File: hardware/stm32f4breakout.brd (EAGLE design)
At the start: 132.1 x 53.3 mm, 18 parts, among them U101 STM32F427VGT6, X101 24MHz

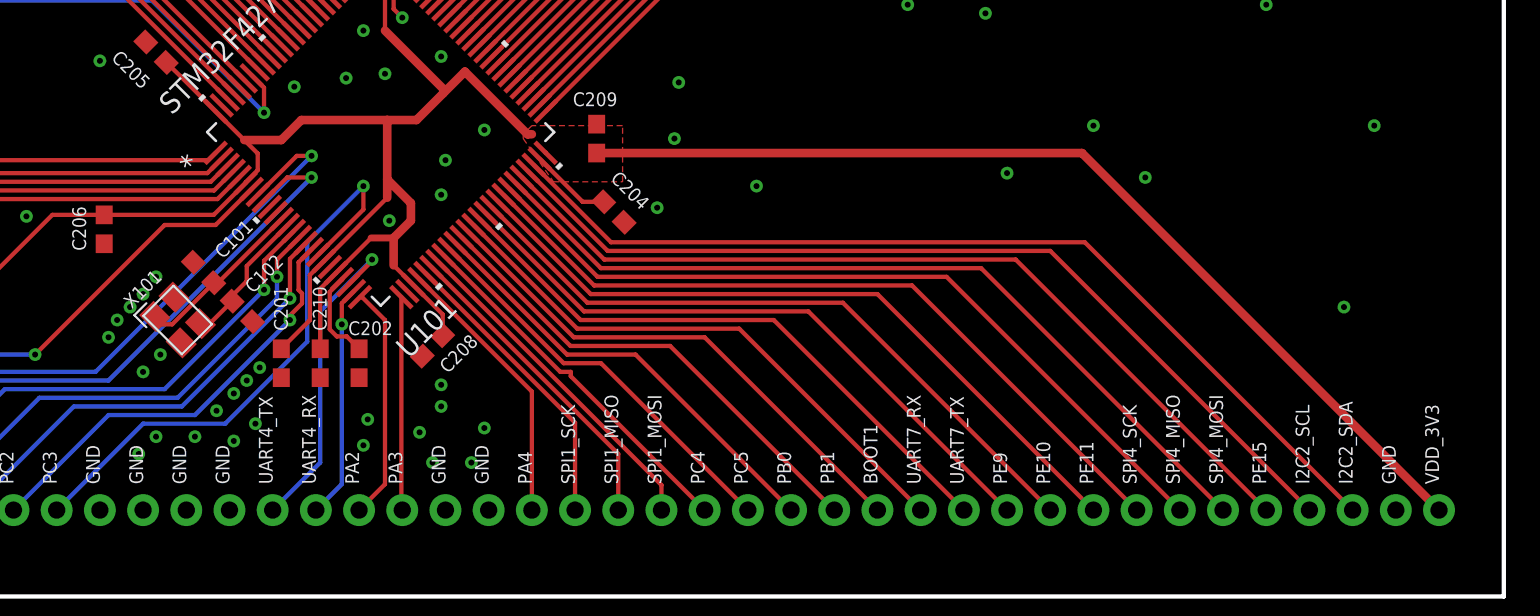
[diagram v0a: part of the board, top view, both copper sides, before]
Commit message: Add 4.7uF decoupling cap
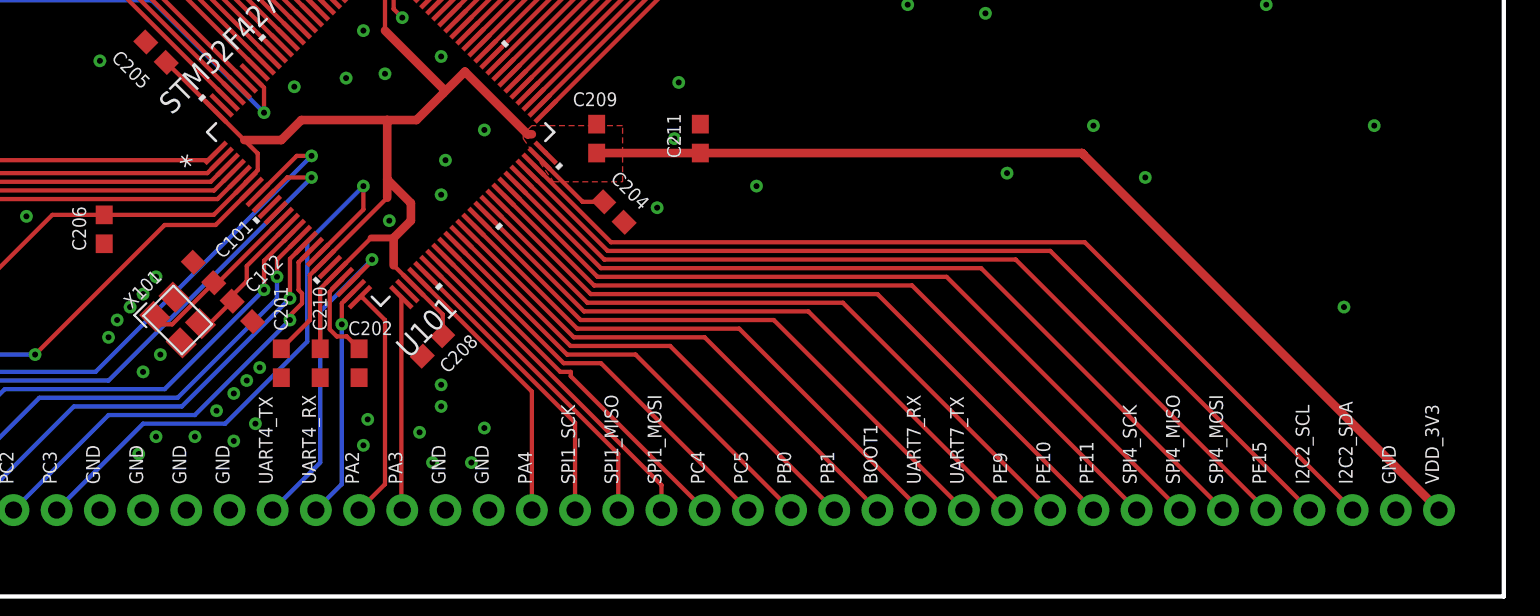
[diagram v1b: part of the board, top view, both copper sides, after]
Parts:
- added C211: 4.7uF, quad:C0603
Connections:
- net GND: now also C211.2
- net VDD_3V3: now also C211.1
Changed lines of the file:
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@@
 <attribute name="NAME" x="62.865" y="15.621" size="0.8128" layer="25" rot="R90"/>
+</element>
+<element name="C211" library="quad" package="C0603" value="4.7uF" x="84.836" y="26.924" smashed="yes" rot="R90">
+<attribute name="NAME" x="83.693" y="25.781" size="0.8128" layer="25" rot="R90"/>
 </element>
 </elements>
@@
 <via x="58.928" y="13.462" extent="1-16" drill="0.35"/>
 <via x="50.038" y="15.24" extent="1-16" drill="0.35"/>
+<contactref element="C211" pad="2"/>
 </signal>
 <signal name="UART4_TX">
@@
 <wire x1="66.802" y1="19.471928125" x2="67.964459375" y2="18.30946875" width="0.254" layer="1"/>
 <wire x1="75.742634375" y1="26.08764375" x2="75.756278125" y2="26.074" width="0.254" layer="1"/>
-<wire x1="78.74" y1="26.074" x2="107.276" y2="26.074" width="0.508" layer="1"/>
-<wire x1="107.276" y1="26.074" x2="128.27" y2="5.08" width="0.508" layer="1"/>
+<wire x1="107.38175625" y1="25.96824375" x2="107.276" y2="26.074" width="0.508" layer="1"/>
+<wire x1="107.38175625" y1="25.96824375" x2="128.27" y2="5.08" width="0.508" layer="1"/>
 <wire x1="67.257353125" y1="37.007634375" x2="66.294" y2="36.04428125" width="0.254" layer="1"/>
 <wire x1="66.294" y1="36.04428125" x2="66.294" y2="33.274" width="0.254" layer="1"/>
@@
 <wire x1="61.8752" y1="16.24578125" x2="60.198" y2="14.56858125" width="0.254" layer="1"/>
 <wire x1="62.484" y1="18.09214375" x2="62.484" y2="14.566" width="0.254" layer="1"/>
-<wire x1="50.171871875" y1="22.44" x2="49.784" y2="22.44" width="0.254" layer="1"/>
-<wire x1="50.171871875" y1="22.44" x2="56.225253125" y2="22.44" width="0.254" layer="1"/>
+<wire x1="49.784" y1="22.44" x2="56.225253125" y2="22.44" width="0.254" layer="1"/>
 <wire x1="56.225253125" y1="22.44" x2="58.105128125" y2="24.319875" width="0.254" layer="1"/>
 <wire x1="63.761984375" y1="18.663021875" x2="63.781996875" y2="18.6430125" width="0.254" layer="1"/>
@@
 <wire x1="36.83" y1="12.534" x2="46.736" y2="22.44" width="0.254" layer="1"/>
 <wire x1="46.736" y1="22.44" x2="49.784" y2="22.44" width="0.254" layer="1"/>
+<contactref element="C211" pad="1"/>
+<wire x1="78.74" y1="26.074" x2="84.836" y2="26.074" width="0.508" layer="1"/>
+<wire x1="84.836" y1="26.074" x2="107.276" y2="26.074" width="0.508" layer="1"/>
+<wire x1="107.276" y1="26.074" x2="107.38175625" y2="25.96824375" width="0.508" layer="1"/>
 <wire x1="58.105128125" y1="24.319875" x2="59.872896875" y2="22.552109375" width="0" layer="19" extent="1-1"/>
 <wire x1="63.761984375" y1="18.663021875" x2="63.40843125" y2="19.016575" width="0" layer="19" extent="1-1"/>

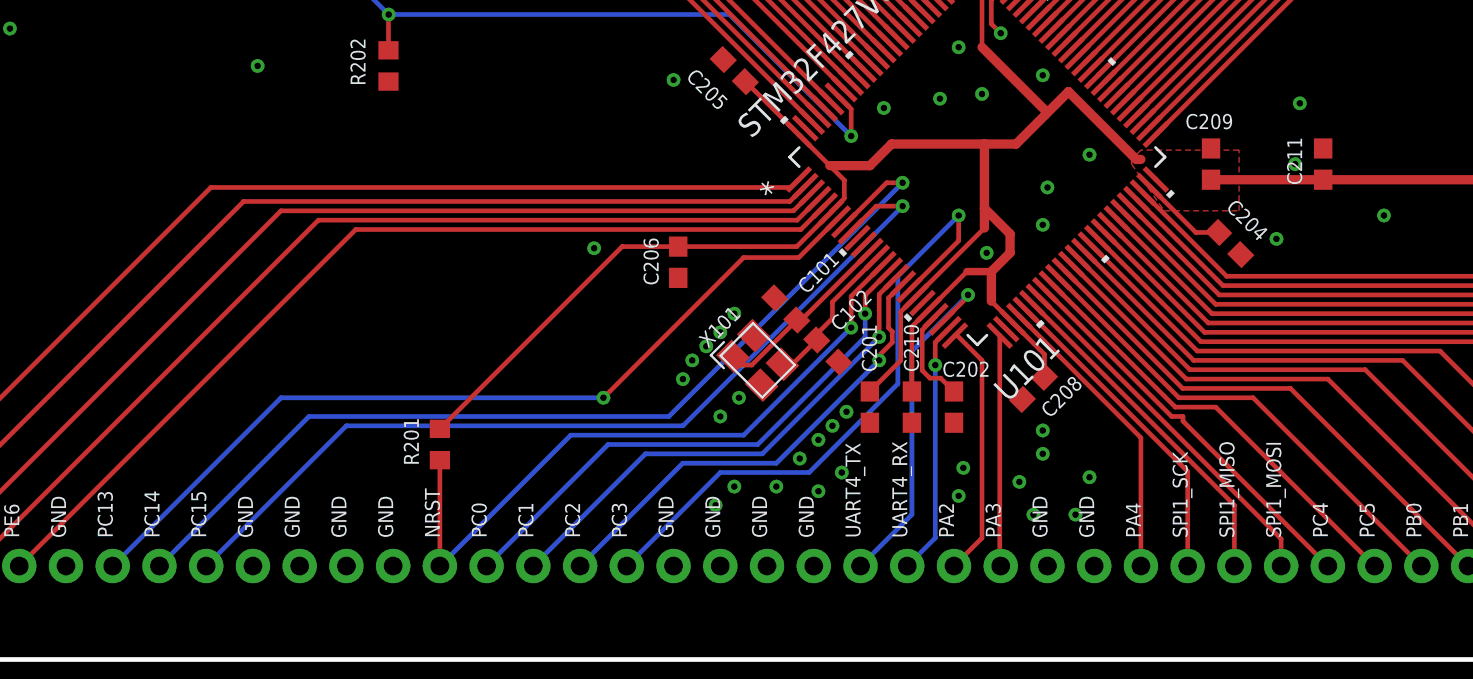
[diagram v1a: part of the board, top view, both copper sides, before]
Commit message: Fix final airwires on breakout, add DRC file
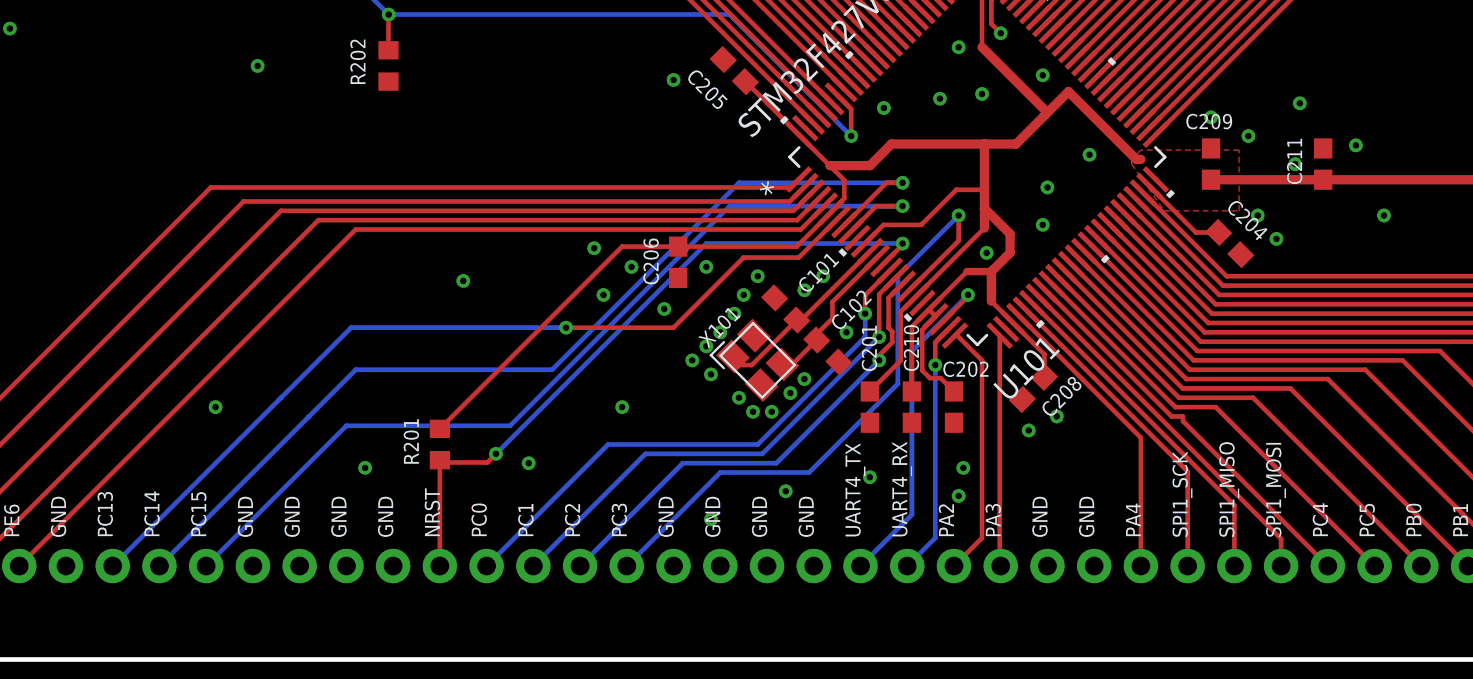
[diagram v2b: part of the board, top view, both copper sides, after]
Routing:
- net VDD_3V3: track 168.0 -> 176.3 mm
- net NRST: track 37.7 -> 37.4 mm, vias 1 -> 2
- net GND: vias 61 -> 72
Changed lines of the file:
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@@
 <via x="50.546" y="16.256" extent="1-16" drill="0.35"/>
 <via x="53.086" y="14.224" extent="1-16" drill="0.35"/>
-<via x="52.07" y="13.208" extent="1-16" drill="0.35"/>
-<via x="52.832" y="9.398" extent="1-16" drill="0.35"/>
-<via x="51.816" y="8.382" extent="1-16" drill="0.35"/>
-<via x="55.118" y="9.398" extent="1-16" drill="0.35"/>
-<via x="56.388" y="10.922" extent="1-16" drill="0.35"/>
-<via x="58.674" y="10.16" extent="1-16" drill="0.35"/>
-<via x="57.404" y="9.144" extent="1-16" drill="0.35"/>
+<via x="55.626" y="9.144" extent="1-16" drill="0.35"/>
+<via x="51.562" y="7.62" extent="1-16" drill="0.35"/>
 <via x="45.212" y="22.352" extent="1-16" drill="0.35"/>
 <via x="65.278" y="10.414" extent="1-16" drill="0.35"/>
 <via x="65.024" y="8.89" extent="1-16" drill="0.35"/>
-<via x="69.596" y="12.446" extent="1-16" drill="0.35"/>
-<via x="69.596" y="11.176" extent="1-16" drill="0.35"/>
-<via x="68.326" y="9.652" extent="1-16" drill="0.35"/>
-<via x="72.136" y="9.906" extent="1-16" drill="0.35"/>
-<via x="71.374" y="7.874" extent="1-16" drill="0.35"/>
-<via x="69.088" y="7.874" extent="1-16" drill="0.35"/>
+<via x="68.834" y="12.446" extent="1-16" drill="0.35"/>
+<via x="70.358" y="13.208" extent="1-16" drill="0.35"/>
 <via x="107.95" y="27.686" extent="1-16" drill="0.35"/>
 <via x="110.998" y="24.638" extent="1-16" drill="0.35"/>
@@
 <wire x1="66.802" y1="35.845175" x2="66.802" y2="34.544" width="0.254" layer="1"/>
 <via x="69.596" y="31.75" extent="1-16" drill="0.35"/>
-<via x="58.166" y="12.7" extent="1-16" drill="0.35"/>
-<via x="57.404" y="11.938" extent="1-16" drill="0.35"/>
-<via x="58.928" y="13.462" extent="1-16" drill="0.35"/>
-<via x="50.038" y="15.24" extent="1-16" drill="0.35"/>
 <contactref element="C211" pad="2"/>
+<via x="51.562" y="15.494" extent="1-16" drill="0.35"/>
+<via x="53.848" y="13.462" extent="1-16" drill="0.35"/>
+<via x="55.88" y="14.478" extent="1-16" drill="0.35"/>
+<via x="56.642" y="15.24" extent="1-16" drill="0.35"/>
+<via x="54.864" y="13.462" extent="1-16" drill="0.35"/>
+<via x="54.102" y="20.828" extent="1-16" drill="0.35"/>
+<via x="53.34" y="19.812" extent="1-16" drill="0.35"/>
+<via x="56.642" y="20.066" extent="1-16" drill="0.35"/>
+<via x="57.658" y="20.828" extent="1-16" drill="0.35"/>
+<via x="58.928" y="17.78" extent="1-16" drill="0.35"/>
+<via x="49.022" y="19.05" extent="1-16" drill="0.35"/>
+<via x="51.308" y="21.336" extent="1-16" drill="0.35"/>
+<via x="47.244" y="21.336" extent="1-16" drill="0.35"/>
+<via x="45.72" y="19.812" extent="1-16" drill="0.35"/>
+<via x="60.198" y="9.906" extent="1-16" drill="0.35"/>
+<via x="78.74" y="29.464" extent="1-16" drill="0.35"/>
+<via x="80.772" y="28.448" extent="1-16" drill="0.35"/>
+<via x="86.614" y="27.94" extent="1-16" drill="0.35"/>
+<via x="81.28" y="24.13" extent="1-16" drill="0.35"/>
+<via x="38.1" y="20.574" extent="1-16" drill="0.35"/>
+<via x="24.638" y="13.716" extent="1-16" drill="0.35"/>
+<via x="32.766" y="10.414" extent="1-16" drill="0.35"/>
+<via x="46.736" y="13.716" extent="1-16" drill="0.35"/>
+<via x="41.656" y="10.668" extent="1-16" drill="0.35"/>
 </signal>
 <signal name="UART4_TX">
@@
 <contactref element="U101" pad="8"/>
 <contactref element="J301" pad="8"/>
-<wire x1="58.812234375" y1="23.61276875" x2="61.107465625" y2="25.908" width="0.254" layer="1"/>
+<wire x1="61.107465625" y1="25.908" x2="58.812234375" y2="23.61276875" width="0.254" layer="1"/>
 <wire x1="61.107465625" y1="25.908" x2="61.976" y2="25.908" width="0.254" layer="1"/>
 <via x="61.976" y="25.908" extent="1-16" drill="0.35"/>
-<wire x1="61.976" y1="25.908" x2="49.276" y2="13.208" width="0.254" layer="16"/>
-<wire x1="29.718" y1="13.208" x2="21.59" y2="5.08" width="0.254" layer="16"/>
-<wire x1="49.276" y1="13.208" x2="29.718" y2="13.208" width="0.254" layer="16"/>
+<wire x1="29.673953125" y1="13.163953125" x2="29.718" y2="13.208" width="0.254" layer="16"/>
+<wire x1="29.673953125" y1="13.163953125" x2="21.59" y2="5.08" width="0.254" layer="16"/>
+<wire x1="53.086" y1="25.908" x2="42.926" y2="15.748" width="0.254" layer="16"/>
+<wire x1="42.926" y1="15.748" x2="32.258" y2="15.748" width="0.254" layer="16"/>
+<wire x1="32.258" y1="15.748" x2="29.673953125" y2="13.163953125" width="0.254" layer="16"/>
+<wire x1="61.976" y1="25.908" x2="53.086" y2="25.908" width="0.254" layer="16"/>
 </signal>
 <signal name="PC15">
@@
 <wire x1="60.544575" y1="24.638" x2="61.976" y2="24.638" width="0.254" layer="1"/>
 <via x="61.976" y="24.638" extent="1-16" drill="0.35"/>
-<wire x1="61.976" y1="24.638" x2="50.038" y2="12.7" width="0.254" layer="16"/>
 <wire x1="31.75" y1="12.7" x2="24.13" y2="5.08" width="0.254" layer="16"/>
-<wire x1="50.038" y1="12.7" x2="31.75" y2="12.7" width="0.254" layer="16"/>
+<wire x1="61.976" y1="24.638" x2="58.42" y2="24.638" width="0.254" layer="16"/>
+<wire x1="58.42" y1="24.638" x2="58.166" y2="24.638" width="0.254" layer="16"/>
+<wire x1="58.42" y1="24.638" x2="52.578" y2="24.638" width="0.254" layer="16"/>
+<wire x1="40.64" y1="12.7" x2="31.75" y2="12.7" width="0.254" layer="16"/>
+<wire x1="52.578" y1="24.638" x2="40.64" y2="12.7" width="0.254" layer="16"/>
 </signal>
 <signal name="CAN1_RX">
@@
 <contactref element="J301" pad="7"/>
 <wire x1="58.45868125" y1="23.966321875" x2="56.336359375" y2="21.844" width="0.254" layer="1"/>
-<via x="45.72" y="14.224" extent="1-16" drill="0.35"/>
-<wire x1="45.72" y1="14.224" x2="28.194" y2="14.224" width="0.254" layer="16"/>
-<wire x1="28.194" y1="14.224" x2="19.05" y2="5.08" width="0.254" layer="16"/>
+<wire x1="28.050115625" y1="14.080115625" x2="28.194" y2="14.224" width="0.254" layer="16"/>
+<wire x1="28.050115625" y1="14.080115625" x2="19.05" y2="5.08" width="0.254" layer="16"/>
 <wire x1="56.336359375" y1="21.844" x2="53.34" y2="21.844" width="0.254" layer="1"/>
-<wire x1="53.34" y1="21.844" x2="45.72" y2="14.224" width="0.254" layer="1"/>
+<wire x1="53.34" y1="21.844" x2="49.53" y2="18.034" width="0.254" layer="1"/>
+<wire x1="49.53" y1="18.034" x2="43.688" y2="18.034" width="0.254" layer="1"/>
+<via x="43.688" y="18.034" extent="1-16" drill="0.35"/>
+<wire x1="43.688" y1="18.034" x2="32.004" y2="18.034" width="0.254" layer="16"/>
+<wire x1="32.004" y1="18.034" x2="28.194" y2="14.224" width="0.254" layer="16"/>
 </signal>
 <signal name="PE2">
@@
 <contactref element="R201" pad="1"/>
 <contactref element="J301" pad="14"/>
-<wire x1="60.93355625" y1="21.49145" x2="59.182" y2="19.73989375" width="0.254" layer="1"/>
-<wire x1="59.182" y1="19.73989375" x2="59.182" y2="18.034" width="0.254" layer="1"/>
-<via x="59.182" y="18.034" extent="1-16" drill="0.35"/>
-<wire x1="59.182" y1="18.034" x2="53.34" y2="12.192" width="0.254" layer="16"/>
-<wire x1="43.942" y1="12.192" x2="36.83" y2="5.08" width="0.254" layer="16"/>
-<wire x1="53.34" y1="12.192" x2="43.942" y2="12.192" width="0.254" layer="16"/>
-<wire x1="36.83" y1="10.834" x2="36.83" y2="5.08" width="0.254" layer="1"/>
+<wire x1="36.83" y1="10.706909375" x2="36.83" y2="10.834" width="0.254" layer="1"/>
+<wire x1="36.83" y1="10.706909375" x2="36.83" y2="5.08" width="0.254" layer="1"/>
+<wire x1="60.93355625" y1="21.49145" x2="61.976" y2="22.53389375" width="0.254" layer="1"/>
+<wire x1="61.976" y1="22.53389375" x2="61.976" y2="22.606" width="0.254" layer="1"/>
+<via x="61.976" y="22.606" extent="1-16" drill="0.35"/>
+<via x="39.878" y="11.176" extent="1-16" drill="0.35"/>
+<wire x1="39.878" y1="11.176" x2="39.408909375" y2="10.706909375" width="0.254" layer="1"/>
+<wire x1="39.408909375" y1="10.706909375" x2="36.83" y2="10.706909375" width="0.254" layer="1"/>
+<wire x1="61.976" y1="22.606" x2="51.308" y2="22.606" width="0.254" layer="16"/>
+<wire x1="51.308" y1="22.606" x2="39.878" y2="11.176" width="0.254" layer="16"/>
 </signal>
 <signal name="VDD_3V3">
@@
 <contactref element="C201" pad="1"/>
 <contactref element="U101" pad="21"/>
-<wire x1="66.424678125" y1="24.523078125" x2="66.424678125" y2="28.0152" width="0.508" layer="1"/>
-<wire x1="63.40843125" y1="19.016575" x2="62.484" y2="18.09214375" width="0.254" layer="1"/>
+<wire x1="66.424678125" y1="25.528484375" x2="66.424678125" y2="24.523078125" width="0.508" layer="1"/>
+<wire x1="66.424678125" y1="25.528484375" x2="66.424678125" y2="28.0152" width="0.508" layer="1"/>
+<wire x1="62.484" y1="18.09214375" x2="63.40843125" y2="19.016575" width="0.254" layer="1"/>
 <wire x1="63.40843125" y1="19.016575" x2="65.47385625" y2="21.082" width="0.254" layer="1"/>
 <wire x1="65.47385625" y1="21.082" x2="66.802" y2="21.082" width="0.4064" layer="1"/>
@@
 <wire x1="84.836" y1="26.074" x2="107.276" y2="26.074" width="0.508" layer="1"/>
 <wire x1="107.276" y1="26.074" x2="107.38175625" y2="25.96824375" width="0.508" layer="1"/>
-<wire x1="58.105128125" y1="24.319875" x2="59.872896875" y2="22.552109375" width="0" layer="19" extent="1-1"/>
-<wire x1="63.761984375" y1="18.663021875" x2="63.40843125" y2="19.016575" width="0" layer="19" extent="1-1"/>
+<wire x1="59.872896875" y1="22.552109375" x2="60.9427875" y2="23.622" width="0.254" layer="1"/>
+<wire x1="60.9427875" y1="23.622" x2="62.992" y2="23.622" width="0.254" layer="1"/>
+<wire x1="62.992" y1="23.622" x2="64.898484375" y2="25.528484375" width="0.254" layer="1"/>
+<wire x1="64.898484375" y1="25.528484375" x2="66.424678125" y2="25.528484375" width="0.254" layer="1"/>
+<wire x1="63.40843125" y1="19.016575" x2="63.761984375" y2="18.663021875" width="0.254" layer="1"/>
 </signal>
 <signal name="VCAP2">
